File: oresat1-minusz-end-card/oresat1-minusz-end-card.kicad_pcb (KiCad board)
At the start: 4 copper layers, 99.8 x 94.6 mm, 90 parts, among them J1 J-SAMTEC-TFM-120-01-L-D-RA, J2 U.FL-R-SMT-1, J3 M55-7101242R, J5 M55-7101242R, Q1 DMP2240UDM, Q2 PMV45EN, Q3 PMV45EN, Q4 PMV45EN, Q5 DMP2240UDM-7, Q6 PMV45EN, Q7 DMP2240UDM-7, U11 MIC842LYC5, U12 MIC842LYC5, U2 MAX7310, U201 TS5A21366, U202 TS5A21366, U203 TS5A21366, U204 TS5A21366

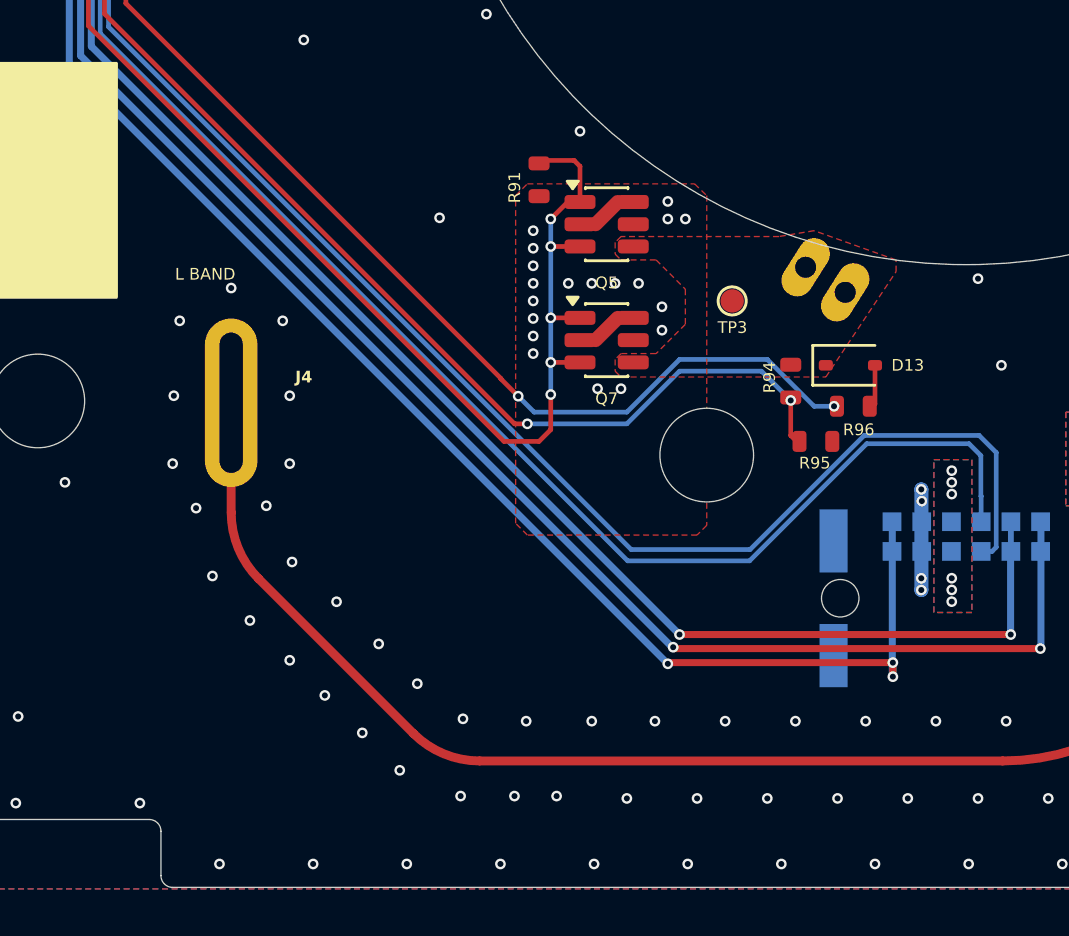
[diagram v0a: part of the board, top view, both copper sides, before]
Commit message: Changes to minus Z
Resolved 2 git issues. Added led test light to deployer circuit to test deployment
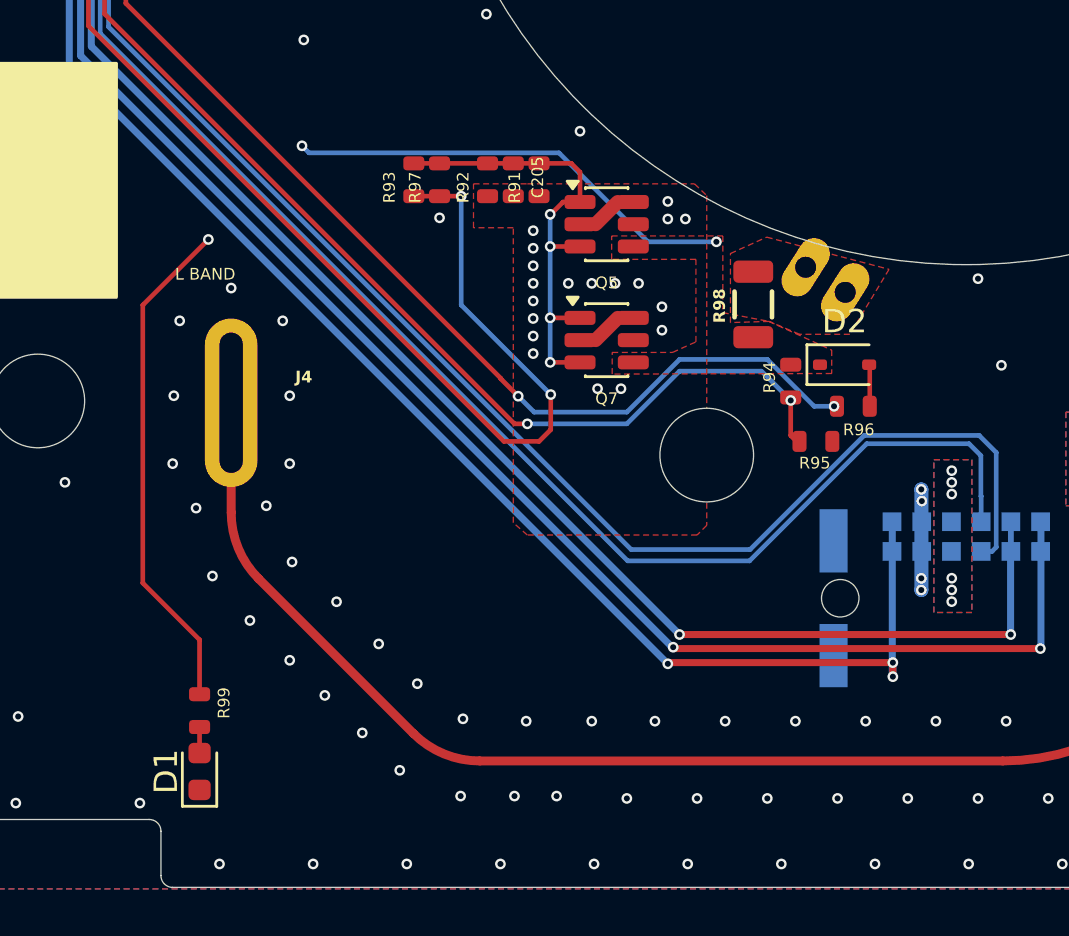
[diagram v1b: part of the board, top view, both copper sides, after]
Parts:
- removed D13: 1N4151WS, Diode_SMD:D_SOD-323
- removed TP3: Test-Point, oresat-misc:TestPoint_Pad_D1.0mm
- added C205: 470n, oresat-passives:0603-C-NOSILK, F.Cu at (129.2, 122.1)
- added D1: RED, LED_SMD:LED_0603_1608Metric, F.Cu at (115.8, 147.3)
- added D2: 1N4151WS, Diode_SMD:D_SOD-323, F.Cu at (143.3, 130.0)
- added R92: 10k, oresat-passives:0603-C-NOSILK, F.Cu at (128.1, 122.1)
- added R93: 10k, oresat-passives:0603-C-NOSILK, F.Cu at (124.9, 122.1)
- added R97: 10k, oresat-passives:0603-C-NOSILK, F.Cu at (126.0, 122.1)
- added R98: 0, oresat-passives:1206-C, F.Cu at (139.4, 127.4)
- added R99: 4.7k, oresat-passives:0603-C-NOSILK, F.Cu at (115.8, 144.8)
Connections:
- Q5 pad 1: Net-(Q2-D) -> Net-(Q5A-G)
- Q5 pad 3: Net-(Q2-D) -> Net-(Q5A-G)
- Q7 pad 1: Net-(Q2-D) -> Net-(Q5A-G)
- Q7 pad 3: Net-(Q2-D) -> Net-(Q5A-G)
- R1 pad 1: /OPD/TURNSTILE_DEPLOY -> Net-(R1-Pad1)
- R91 pad 2: Net-(Q2-D) -> Net-(Q5A-G)
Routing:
- net /OPD/TURNSTILE_DEPLOY: track 0.62 -> 46.6 mm, vias 0 -> 3
- net Net-(Q5A-G): track 0.00 -> 20.2 mm, vias 0 -> 4
- net Net-(Q2-D): track 87.7 -> 83.6 mm, vias 7 -> 4
- net Net-(D1-A): track 0.00 -> 1.11 mm
- net Net-(R1-Pad1): track 0.00 -> 0.62 mm
- added copper zone on F.Cu, net Net-(R1-Pad1)

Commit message: Routine push
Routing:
- net Net-(Q2-D): track 83.6 -> 81.7 mm
- net /OPD/TURNSTILE_DEPLOY: track 46.6 -> 45.5 mm, vias 3 -> 2
- net /MX_UART_TX: track 102.3 -> 103.3 mm
- net /MX_UART_RX: track 102.1 -> 103.1 mm
- net /OPD/READ_ANTENNAS: track 91.9 -> 91.2 mm
- net /CAN1_H: track 151.4 -> 152.1 mm
- net /CAN1_L: track 155.4 -> 156.0 mm

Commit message: Routine Push
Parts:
- removed C202, C204: 100n, oresat-passives:0603-C-NOSILK
- removed U202, U204: TS5A21366, Package_SO:VSSOP-8_2.3x2mm_P0.5mm
- CM1, CM2, CM3: value 2477330-1 -> 733000020
- moved D1 0.55 mm to (115.7, 147.9)
- moved R99 0.55 mm to (115.7, 145.3)
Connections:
- U2 pad 10: /OPD/PY_UART_EN -> unconnected-(U2-IO5-Pad10)
- U2 pad 12: /OPD/MY_UART_EN -> unconnected-(U2-IO7-Pad12)
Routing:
- net /OPD/MY_UART_EN: track 27.6 -> 0.00 mm, vias 2 -> 0
- net /OPD/PY_UART_EN: track 23.1 -> 0.00 mm, vias 2 -> 0
- net /C3-UART-TX: track 28.3 -> 17.1 mm
- net /C3-UART-RX: track 19.5 -> 9.81 mm
- net /OPD/TURNSTILE_DEPLOY: track 45.5 -> 46.1 mm
